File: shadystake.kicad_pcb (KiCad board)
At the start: 2 copper layers, 96.8 x 181.5 mm, 19 parts, among them J1 6P6C, J2 6P6C, J3 6P6C, J4 6P6C, J5 6P6C, J6 6P6C, J7 8P8C

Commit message: DRC 0
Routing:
- net /TIP4: track 100.9 -> 100.3 mm
- net Earth_Protective: track 0.00 -> 0.51 mm

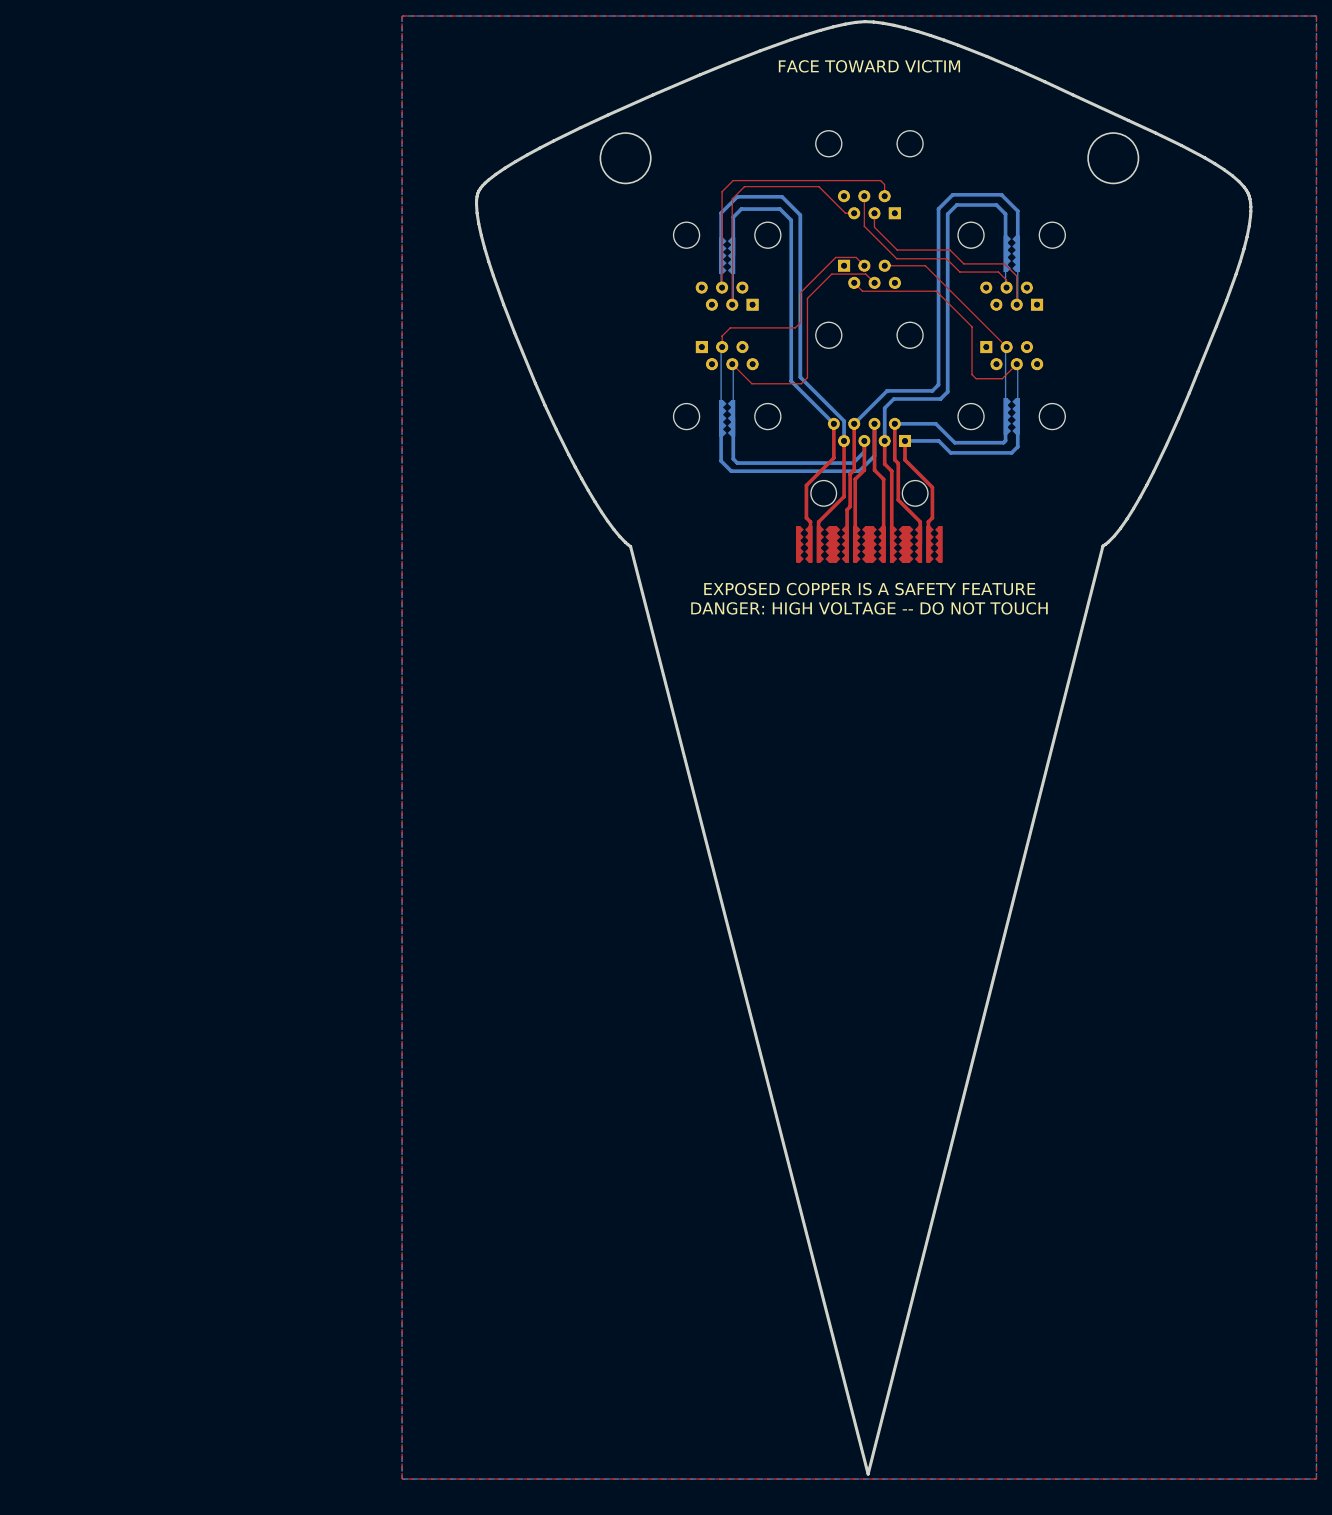
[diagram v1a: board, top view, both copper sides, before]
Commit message: Add QR code, Shadytel logo, and "call operator" note
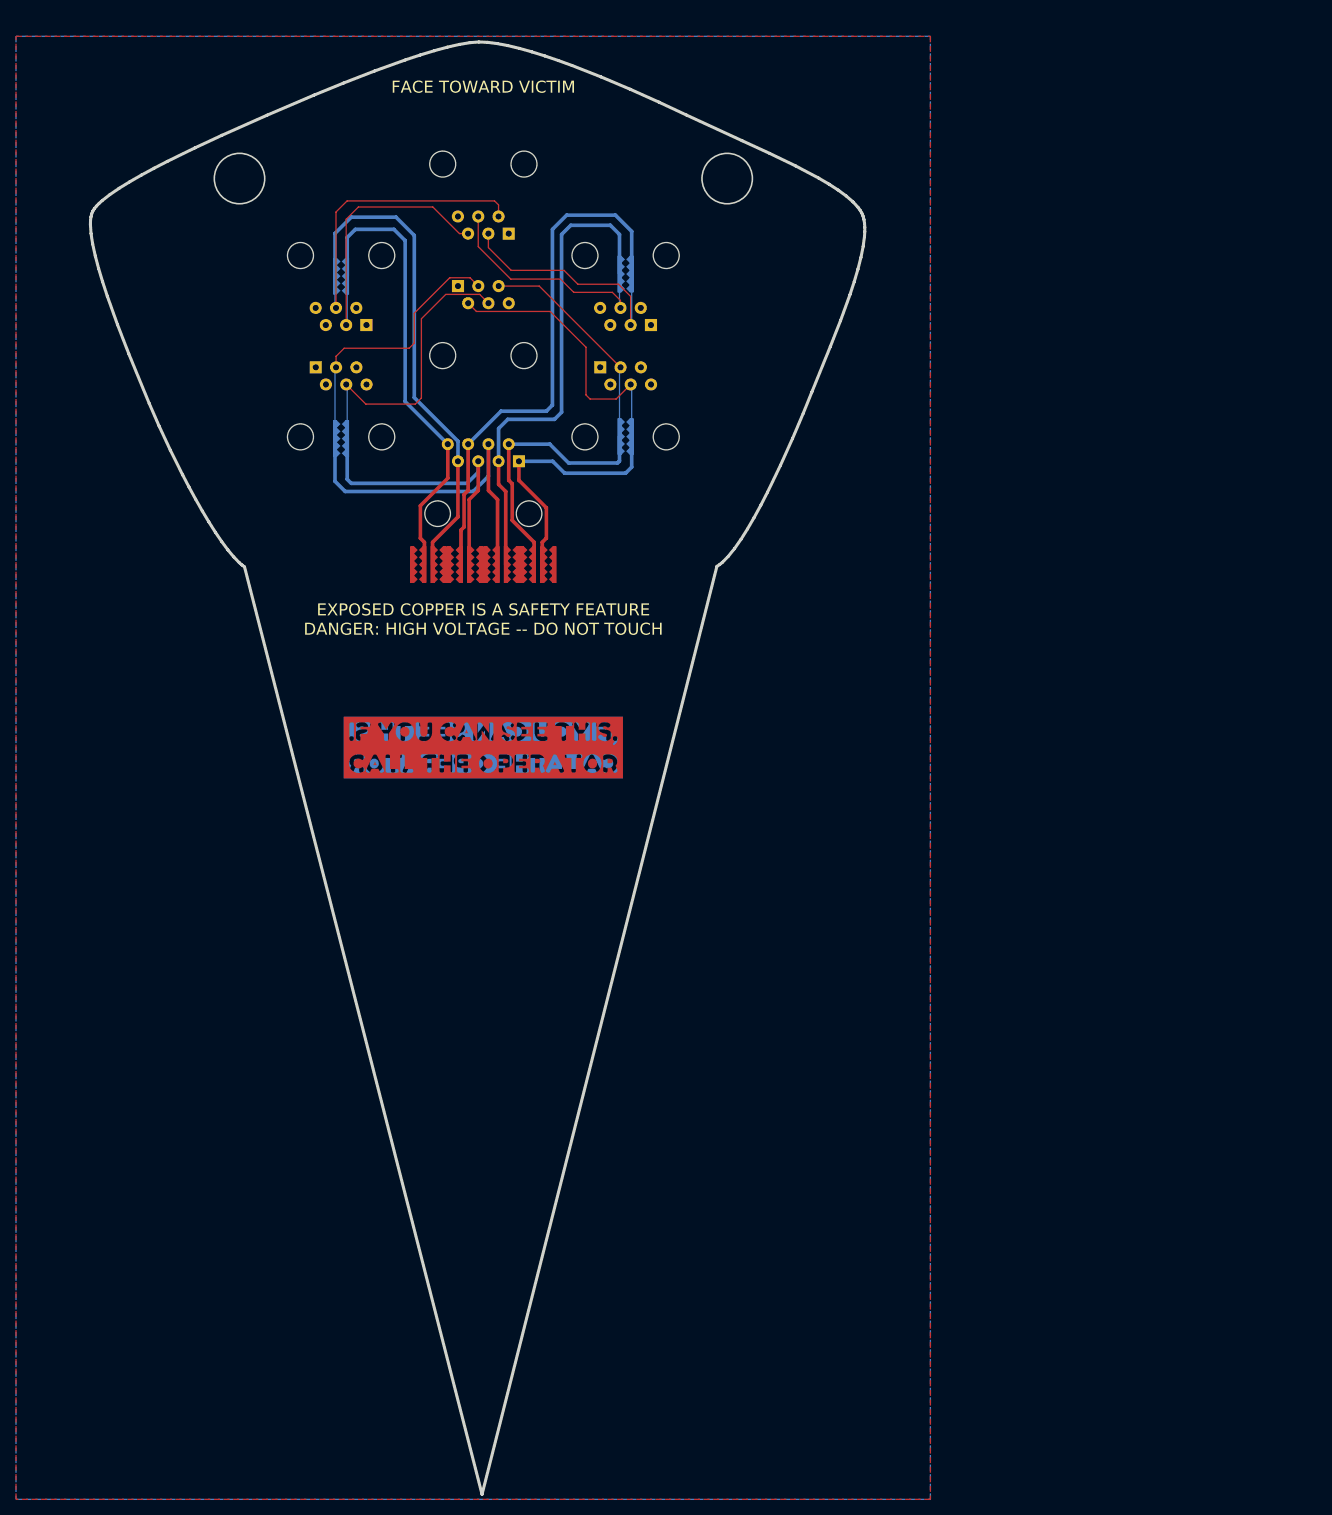
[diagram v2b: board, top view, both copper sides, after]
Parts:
- added kibuzzard-62B55205: G***, kibuzzard-62B55205, F.Cu at (86.4, 104.1)
- added kibuzzard-62B55205: G***, kibuzzard-62B55205, B.Cu at (86.4, 104.1)
- added kibuzzard-62B55316: G***, kibuzzard-62B55316, F.Cu at (104.1, 81.3)
- added svg2mod: G***, Shadystake:fap, F.Cu at (116.3, 38.8)
- added svg2mod: G***, Shadystake:fap, F.Cu at (43.9, 38.8)
- added svg2mod: G***, Shadystake:shadytel, B.Cu at (112.8, 78.7)
- moved E1 48.3 mm to (85.3, 81.3)
- moved E10 48.3 mm to (104.1, 65.3)
- moved E11 48.3 mm to (104.1, 45.0)
- moved E12 48.3 mm to (68.6, 45.2)
- moved E4 48.3 mm to (91.9, 81.3)
- moved E7 48.3 mm to (80.8, 81.3)
- moved E8 48.3 mm to (78.2, 81.3)
- moved E9 48.3 mm to (68.6, 65.5)
- moved J1 48.3 mm to (65.4, 56.4)
- moved J4 48.3 mm to (71.8, 51.5)
- moved E2 48.3 mm to (87.4, 81.3)
- moved E3 48.3 mm to (94.5, 81.3)
- moved E5 48.3 mm to (89.9, 81.3)
- moved E6 48.3 mm to (82.8, 81.3)
- moved J2 48.3 mm to (101.0, 56.4)
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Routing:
- net Earth_Protective: track 0.51 -> 0.00 mm

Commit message: Add shadytel labs logo and "scan for service"
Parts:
- added svg2mod: G***, Shadystake:shadytel_labs, F.Cu at (62.2, 73.7)
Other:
- board text added: "SCAN FOR SERVICE"

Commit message: More updates
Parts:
- added TP1: TestPoint, Shadystake:TP, B.Cu at (50.7, 72.4)
- added TP2: TestPoint, Shadystake:TP, B.Cu at (53.7, 77.3)
- added TP3: TestPoint, Shadystake:TP, B.Cu at (118.2, 77.3)
- added TP4: TestPoint, Shadystake:TP, B.Cu at (121.0, 72.2)
- added TP5: TestPoint, Shadystake:TP, B.Cu at (124.7, 63.8)
- added TP6: TestPoint, Shadystake:TP, B.Cu at (126.8, 58.5)
- added TP7: TestPoint, Shadystake:TP, B.Cu at (44.0, 58.0)
- added TP8: TestPoint, Shadystake:TP, B.Cu at (46.5, 63.4)
- added svg2mod: G***, Shadystake:ground, F.Cu at (81.3, 162.8)
- added svg2mod: G***, Shadystake:shock_warning, B.Cu at (118.9, 59.2)
- added svg2mod: G***, Shadystake:shock_warning, B.Cu at (55.9, 58.7)
- added svgemod: G***, Shadystake:ground, B.Cu at (90.9, 162.8)
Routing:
- net /TIP2: track 69.5 -> 104.8 mm
- net /TIP1: track 74.6 -> 109.0 mm
- net /RING2: track 62.5 -> 96.2 mm
- net /RING1: track 80.2 -> 113.8 mm
- net /TIP4: track 100.3 -> 129.9 mm
- net /TIP3: track 91.0 -> 120.3 mm
- net /RING4: track 94.1 -> 122.9 mm
- net /RING3: track 98.8 -> 123.8 mm
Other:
- board text added: "** PCB ORDER NUM **"
- board text added: "THIS SIDE PHONE COMPANY USE ONLY!"

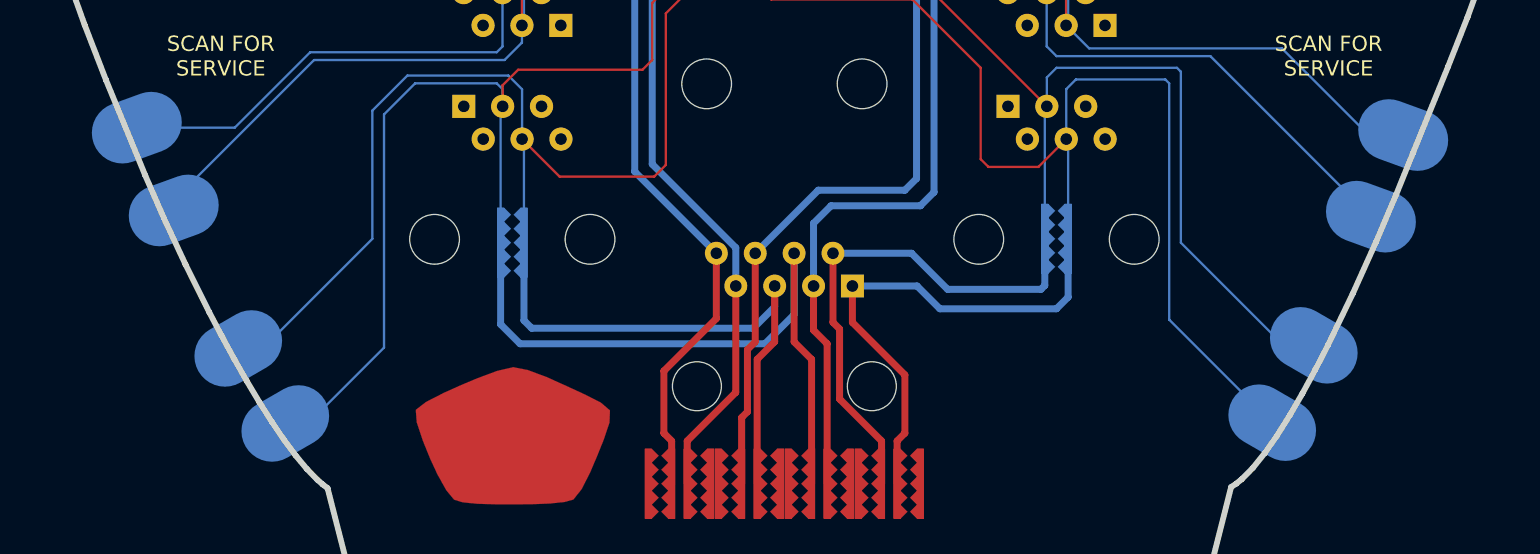
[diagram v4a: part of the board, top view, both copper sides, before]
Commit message: TP footprint update
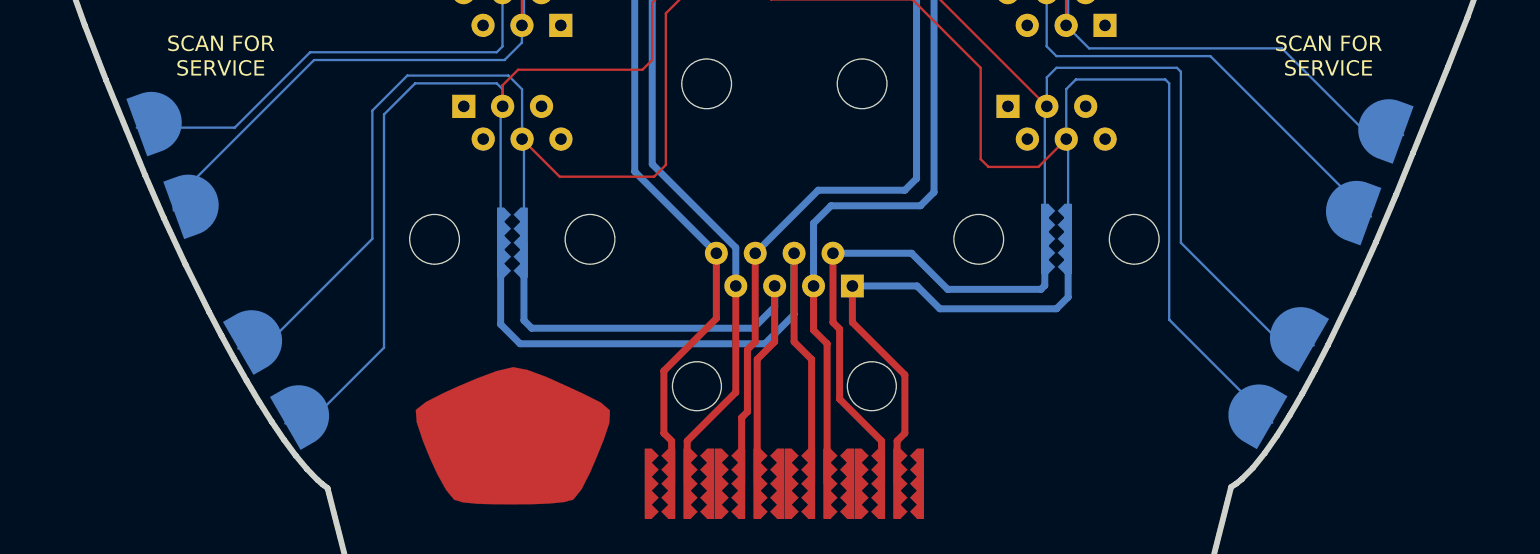
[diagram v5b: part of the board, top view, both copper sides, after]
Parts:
- turned TP3 to -30 degrees
- turned TP4 to -30 degrees

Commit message: TP fine adjustment
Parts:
- moved TP6 0.34 mm to (127.1, 58.6), turned to -22 degrees
- moved TP5 0.29 mm to (125.0, 64.0), turned to -23 degrees
- moved TP4 0.14 mm to (121.1, 72.2), turned to -27 degrees
- moved TP1 0.12 mm to (50.8, 72.4), turned to -151 degrees
- moved TP2 0.06 mm to (53.8, 77.3), turned to -145 degrees
- turned TP3 to -33 degrees
- turned TP7 to -158 degrees
- turned TP8 to -156 degrees
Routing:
- net /RING3: track 123.8 -> 121.6 mm
- net /RING2: track 96.2 -> 94.2 mm
- net /TIP1: track 109.0 -> 107.4 mm
- net /RING1: track 113.8 -> 112.3 mm
- net /TIP4: track 129.9 -> 128.8 mm
- net /TIP3: track 120.3 -> 119.4 mm
- net /RING4: track 122.9 -> 122.2 mm
